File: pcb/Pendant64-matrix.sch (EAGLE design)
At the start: 84 parts, among them U2 MMA8653FC

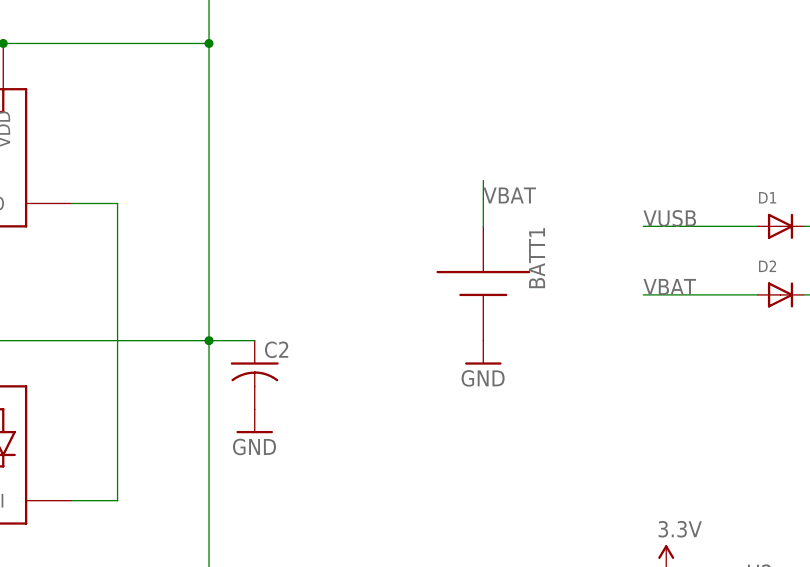
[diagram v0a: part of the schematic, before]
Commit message: added a second AAA battery, relocated wifi to center of board
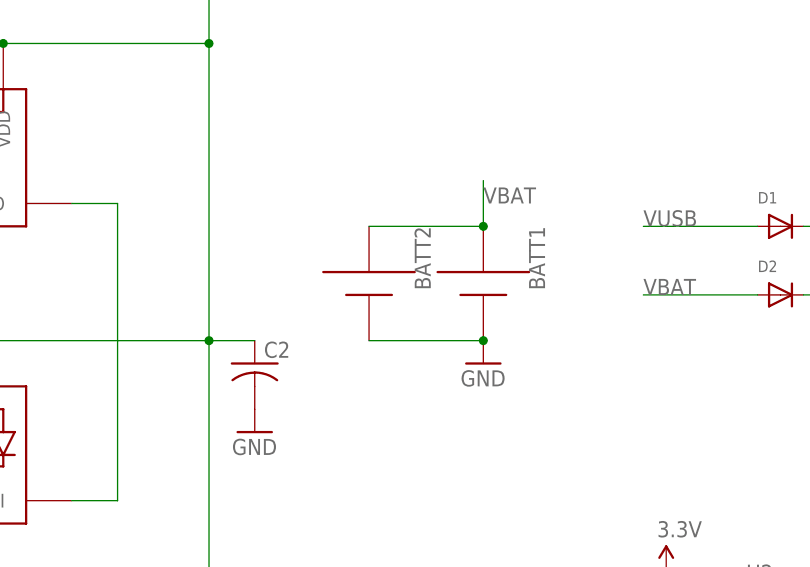
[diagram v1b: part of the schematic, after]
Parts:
- added BATT2: AAA, adafruit:AAA
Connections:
- net GND: now also BATT2.+
- net VBAT: now also BATT2.-
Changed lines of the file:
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@@
 <part name="JP7" library="adafruit" deviceset="PINHD-1X1" device=""/>
 <part name="GND1" library="supply1" deviceset="GND" device=""/>
+<part name="BATT2" library="adafruit" deviceset="AAA" device=""/>
 </parts>
 <sheets>
@@
 <instance part="JP7" gate="G$1" x="307.34" y="50.8" rot="MR0"/>
 <instance part="GND1" gate="1" x="320.04" y="43.18"/>
+<instance part="BATT2" gate="G$1" x="276.86" y="165.1" rot="R270"/>
 </instances>
 <busses>
@@
 <pinref part="BATT1" gate="G$1" pin="+"/>
 <pinref part="GND3" gate="1" pin="GND"/>
+<pinref part="BATT2" gate="G$1" pin="+"/>
+<wire x1="276.86" y1="160.02" x2="289.56" y2="160.02" width="0.1524" layer="91"/>
+<junction x="289.56" y="160.02"/>
 </segment>
 <segment>
@@
 <wire x1="289.56" y1="172.72" x2="289.56" y2="177.8" width="0.1524" layer="91"/>
 <label x="289.56" y="175.26" size="1.778" layer="95"/>
-</segment>
-<segment>
+<pinref part="BATT2" gate="G$1" pin="-"/>
+<wire x1="276.86" y1="172.72" x2="289.56" y2="172.72" width="0.1524" layer="91"/>
+<junction x="289.56" y="172.72"/>
+</segment>
+<segment>
